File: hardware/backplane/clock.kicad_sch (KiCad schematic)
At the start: 4 parts, among them U6 Si5351A-B-GT, Y1 STDCRG2-27M

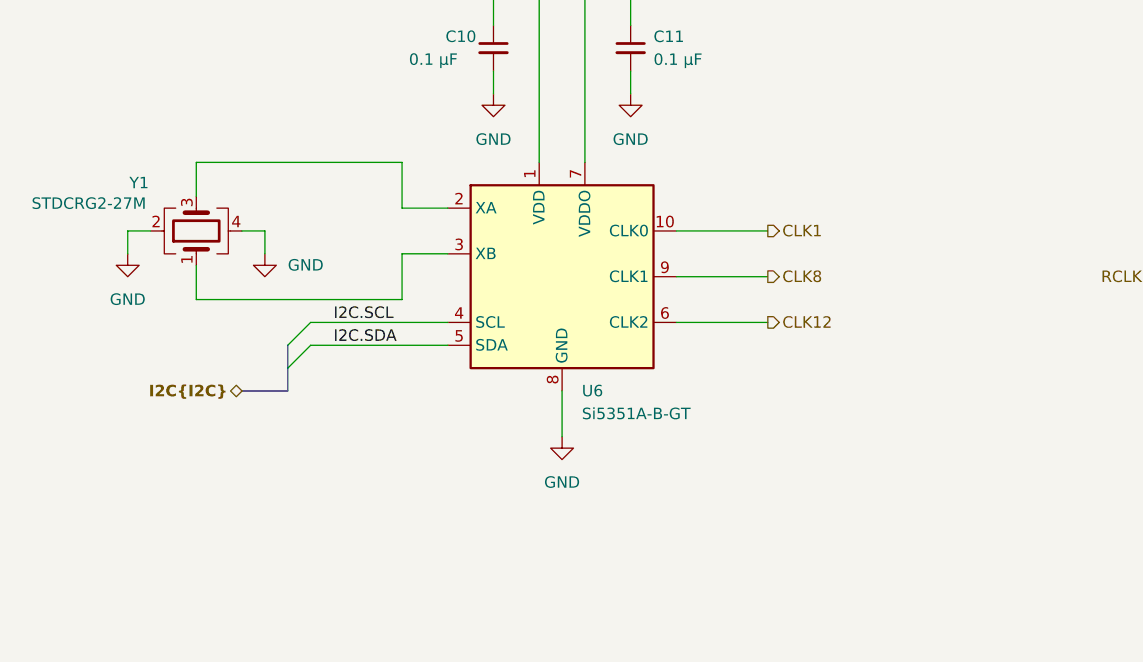
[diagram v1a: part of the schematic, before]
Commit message: feat: Assign footprints, add testpoints
 * Verify all footprints are assigned.
 * Create testpoints for key signals.
 * Reorganize component libraries.
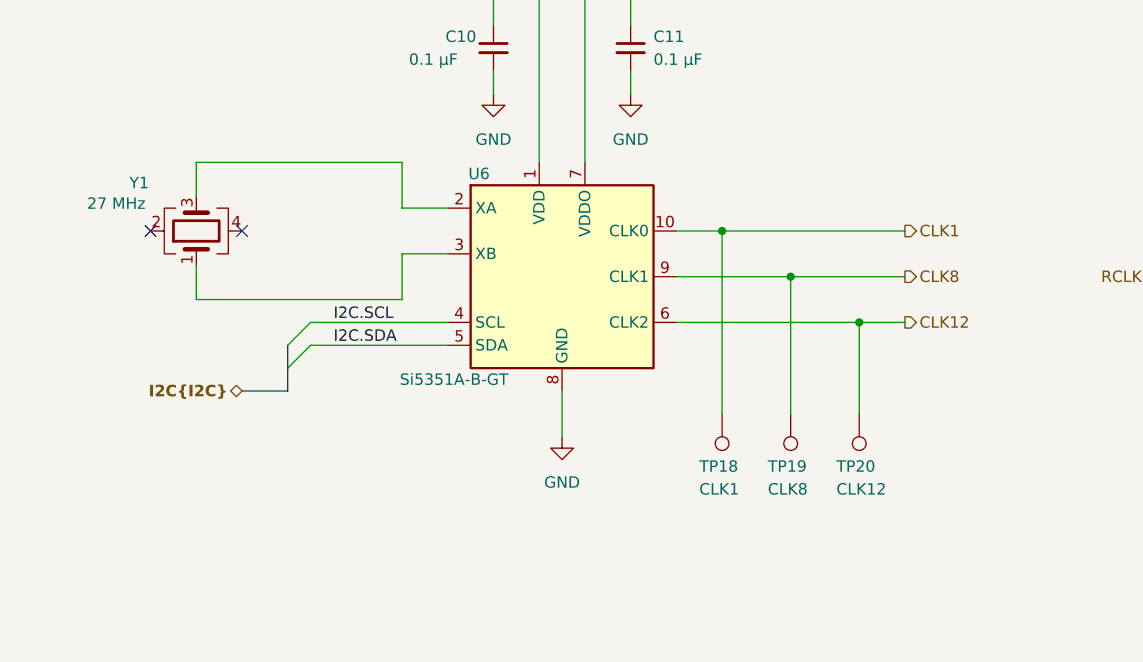
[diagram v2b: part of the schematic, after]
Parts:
- added TP18: CLK1, TestPoint:TestPoint_Pad_D1.0mm, symbol Connector:TestPoint
- added TP19: CLK8, TestPoint:TestPoint_Pad_D1.0mm, symbol Connector:TestPoint
- added TP20: CLK12, TestPoint:TestPoint_Pad_D1.0mm, symbol Connector:TestPoint
- C10, C11: footprint (none) -> Capacitor_SMD:C_0402_1005Metric; Part Number (none) -> GRM155R71C104KA88J
- U6: Part Number (none) -> SI5351A-B-GTR
- Y1: value STDCRG2-27M -> 27 MHz; footprint (none) -> Crystal:Crystal_SMD_3225-4Pin_3.2x2.5mm; Part Number (none) -> STDCRG2-27M
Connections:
- net CLK1: now also TP18.1
- net CLK12: now also TP20.1
- net CLK8: now also TP19.1
- net GND: no longer Y1.2, Y1.4
- no-connect marks 0 -> 2

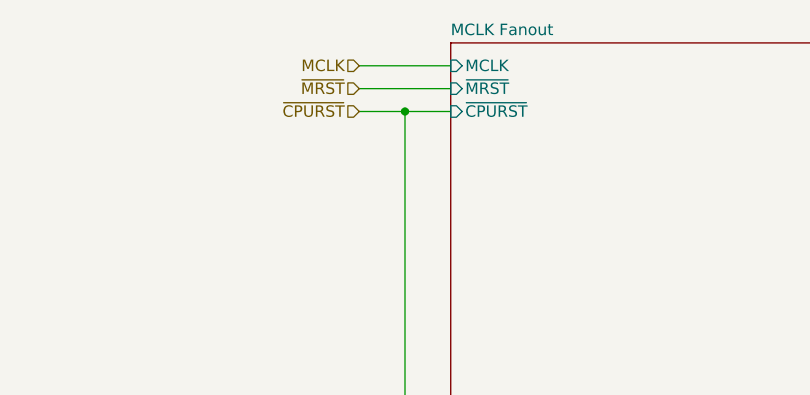
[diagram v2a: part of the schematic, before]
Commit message: feat: Apply bus arch changes to backplane schematic
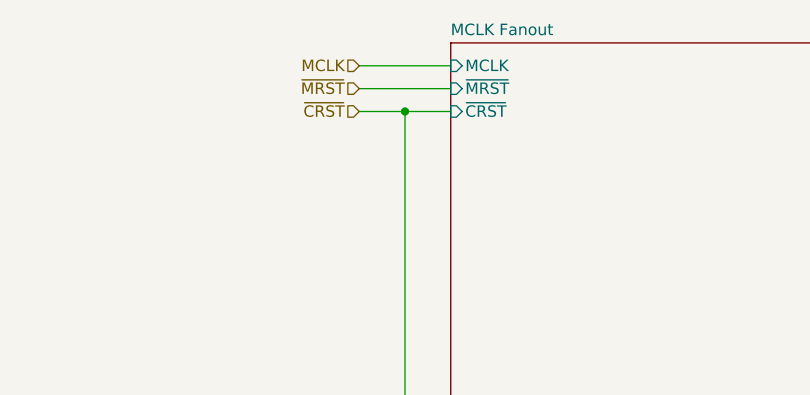
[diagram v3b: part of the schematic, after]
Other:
- sheet MCLK Fanout ports: added ~{CRST}; removed ~{CPURST}
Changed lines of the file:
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@@
 		)
 	)
-	(hierarchical_label "~{CPURST}"
+	(hierarchical_label "~{CRST}"
 		(shape input)
 		(at 154.94 46.99 180)
@@
 			)
 		)
-		(pin "~{CPURST}" input
+		(pin "~{CRST}" input
 			(at 165.1 46.99 180)
 			(effects
